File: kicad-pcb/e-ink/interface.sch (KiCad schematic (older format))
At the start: 0 parts

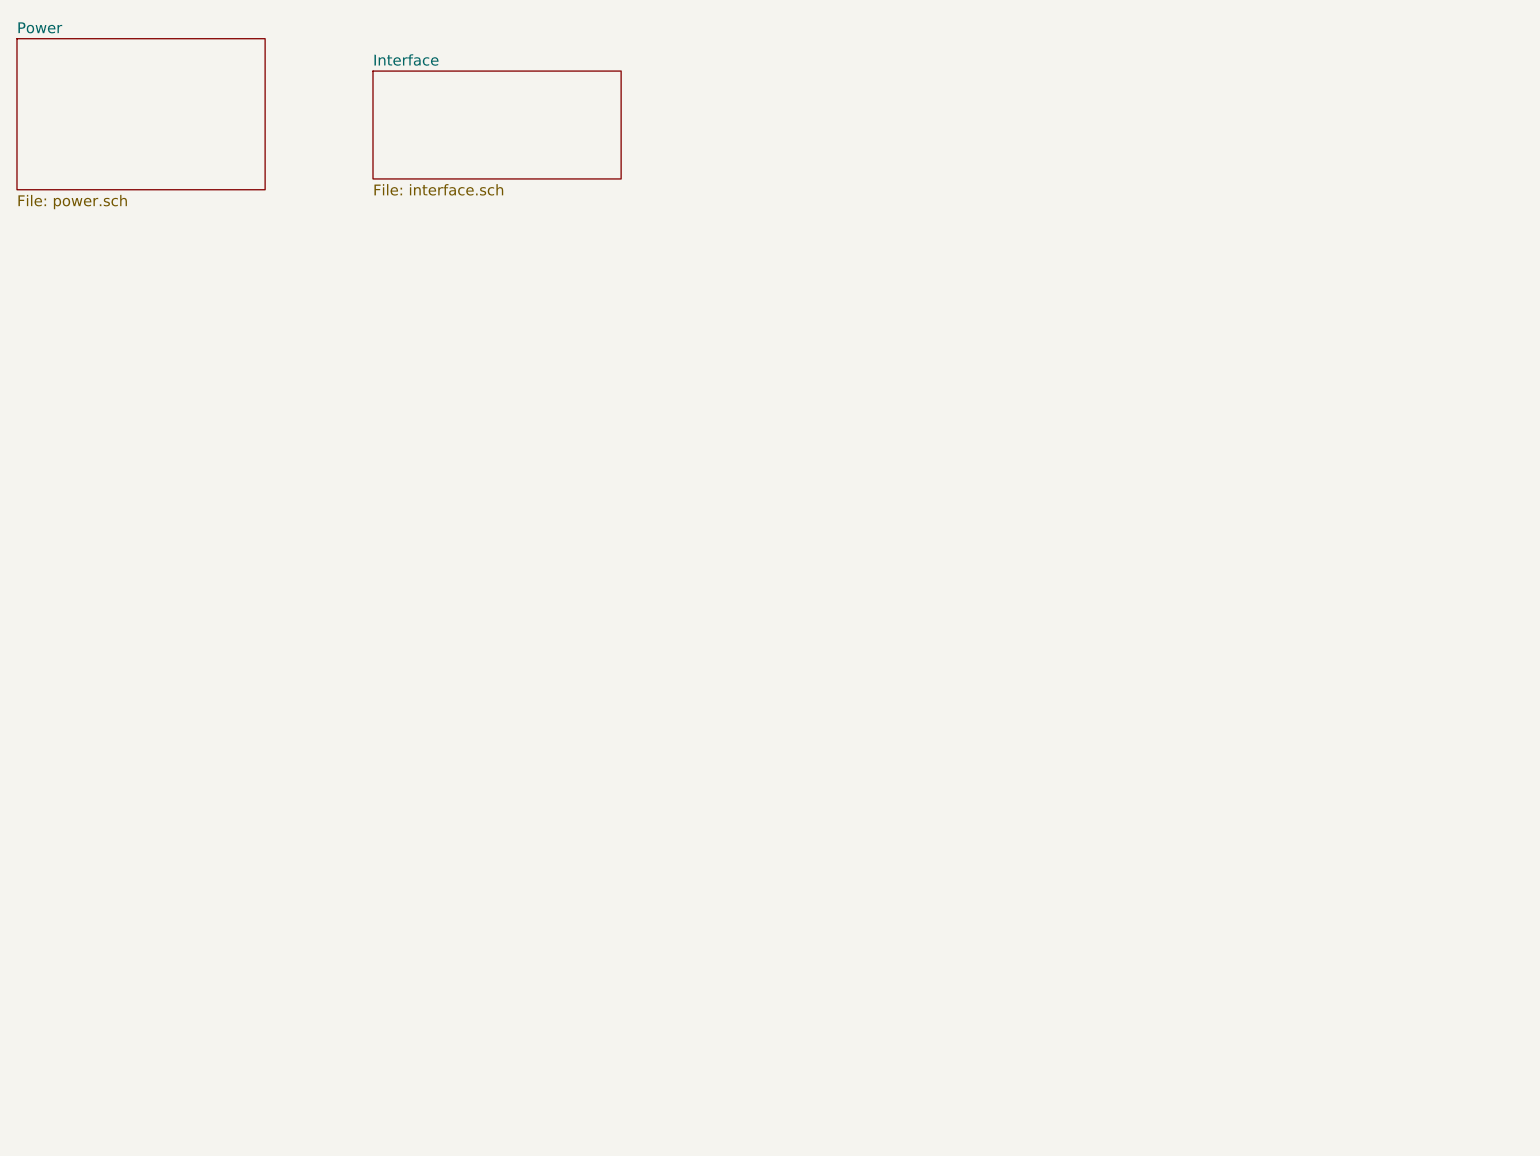
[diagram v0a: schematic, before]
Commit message: reorganized schems and added a note about buffer
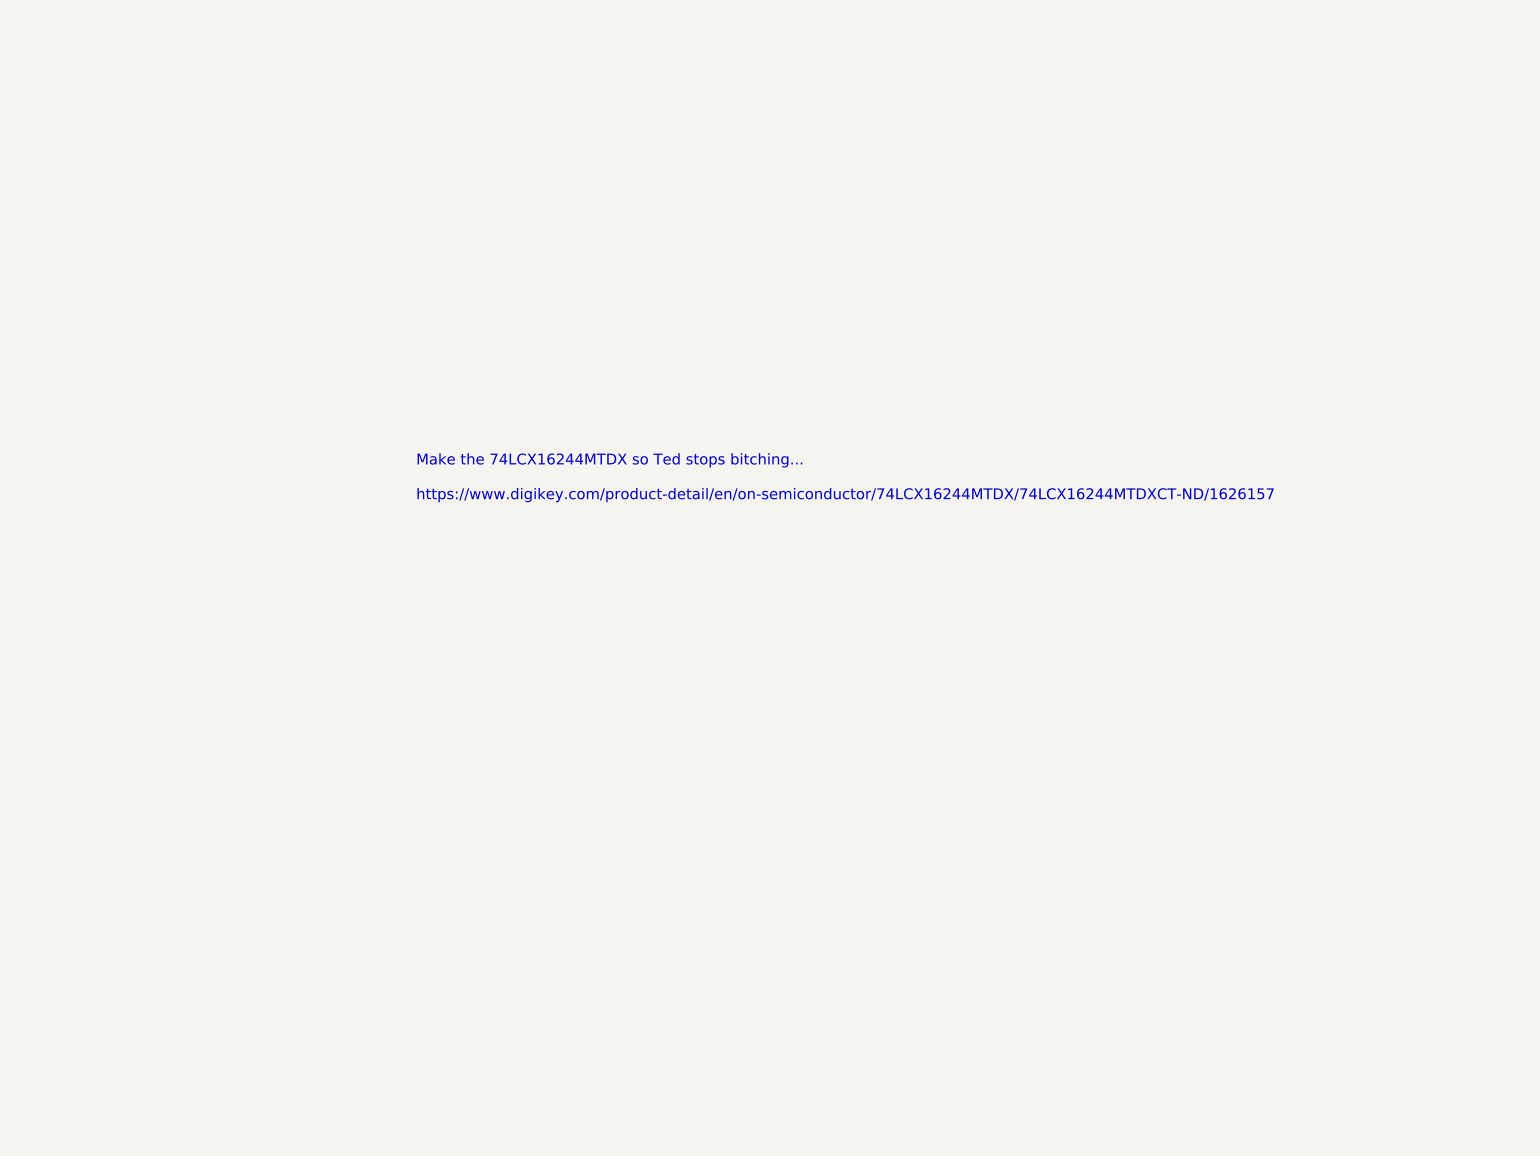
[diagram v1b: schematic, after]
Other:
- note added: "Make the 74LCX16244MTDX so Ted stops bitching...\n\nhttps://www.digikey.com/product-detail/en/on-semiconductor/74LCX16244MTDX/74LCX16244MTDXCT-ND/1626157"
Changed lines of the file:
@@
 $Descr USLetter 11000 8500
 encoding utf-8
-Sheet 1 3
+Sheet 3 3
 Title "E-Ink Bullshit"
 Date "2019-02-03"
@@
 Comment4 ""
 $EndDescr
-$Sheet
-S 1400 950  1150 700
-U 5C57D13E
-F0 "Power" 50
-F1 "power.sch" 50
-$EndSheet
-$Sheet
-S 3050 1100 1150 500
-U 5C5A66EB
-F0 "Interface" 50
-F1 "interface.sch" 50
-$EndSheet
+Text Notes 3250 3100 0    50   ~ 0
+Make the 74LCX16244MTDX so Ted stops bitching...\n\nhttps://www.digikey.com/product-detail/en/on-semiconductor/74LCX16244MTDX/74LCX16244MTDXCT-ND/1626157
 $EndSCHEMATC

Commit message: added 74LCX16244
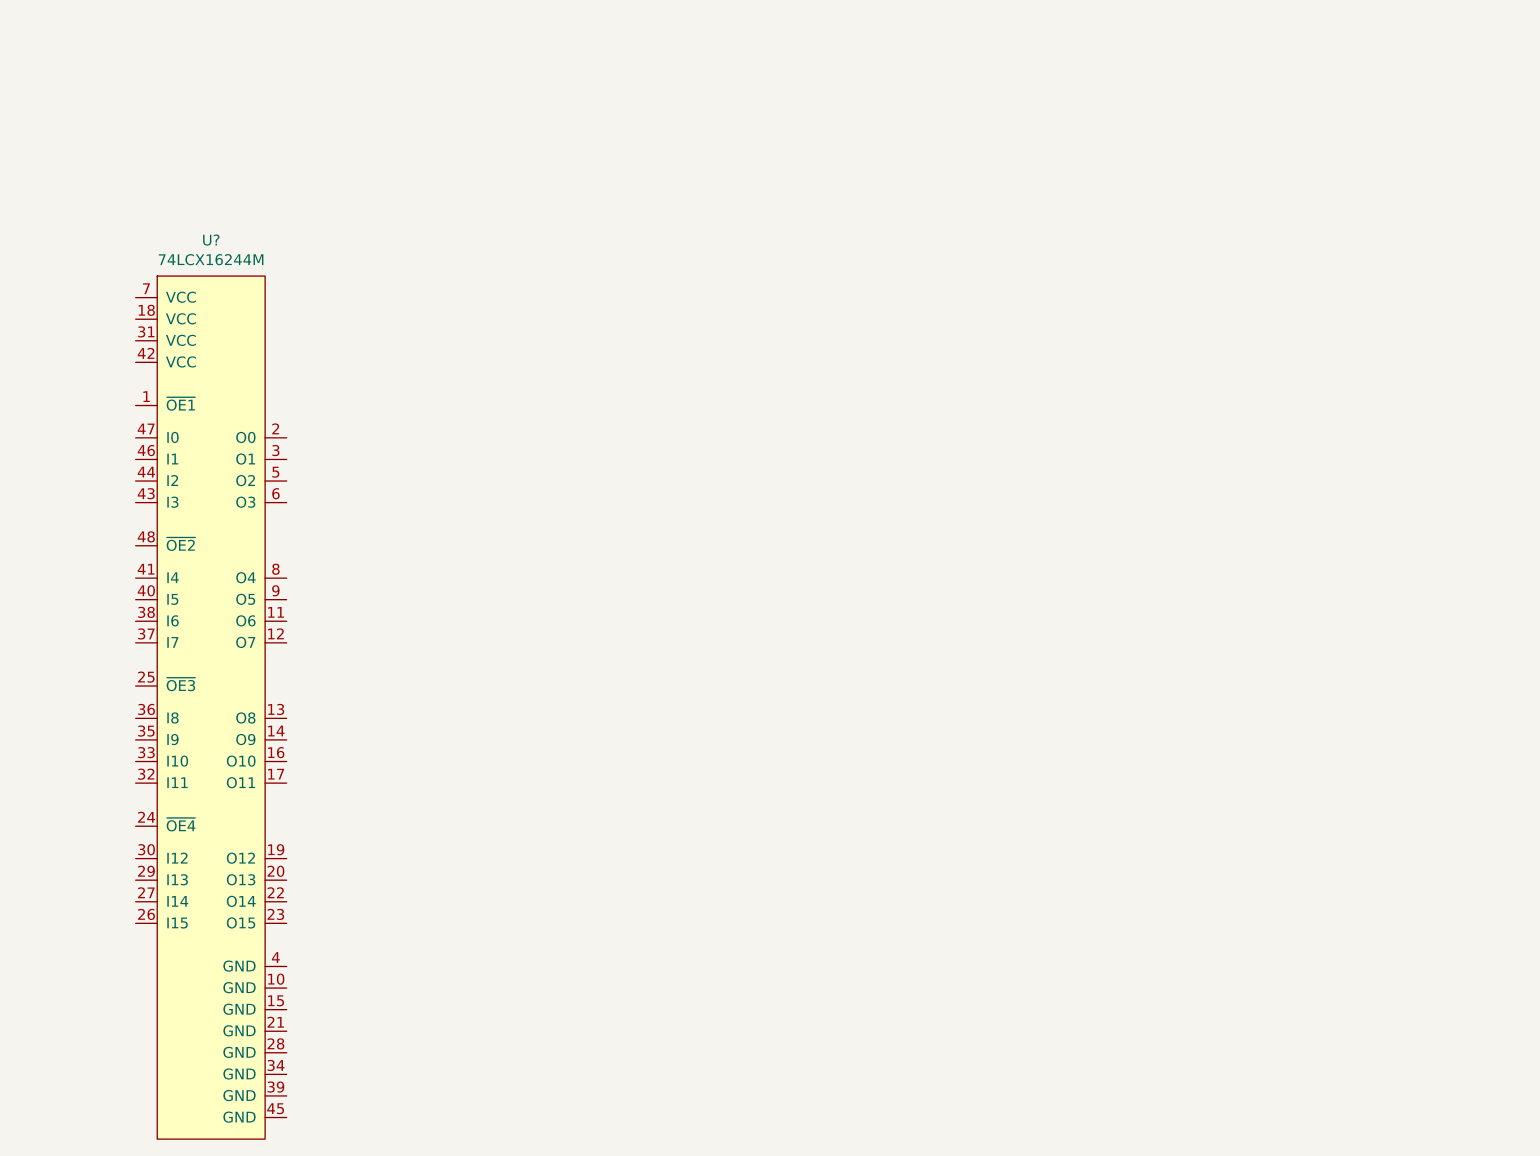
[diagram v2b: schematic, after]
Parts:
- added U?: 74LCX16244M, symbol custom:74LCX16244M
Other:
- note removed: "Make the 74LCX16244MTDX so Ted stops bitching...\n\nhttps://www.digikey.com/product-detail/en/on-semiconductor/74LCX16244MTDX/74LCX16244MTDXCT-ND/1626157"
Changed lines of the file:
@@
 Comment4 ""
 $EndDescr
-Text Notes 3250 3100 0    50   ~ 0
-Make the 74LCX16244MTDX so Ted stops bitching...\n\nhttps://www.digikey.com/product-detail/en/on-semiconductor/74LCX16244MTDX/74LCX16244MTDXCT-ND/1626157
+$Comp
+L custom:74LCX16244M U?
+U 1 1 5C73E360
+P 2050 2050
+F 0 "U?" H 2300 2215 50  0000 C CNN
+F 1 "74LCX16244M" H 2300 2124 50  0000 C CNN
+F 2 "" H 1500 -650 50  0001 C CNN
+F 3 "https://www.onsemi.com/pub/Collateral/74LCX16244-D.pdf" H 2050 -2300 50  0001 C CNN
+	1    2050 2050
+	1    0    0    -1
+$EndComp
 $EndSCHEMATC
